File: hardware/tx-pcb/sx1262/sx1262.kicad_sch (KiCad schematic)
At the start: 13 parts, among them U1 SX1262IMLTRT, X1 CS11336-32M

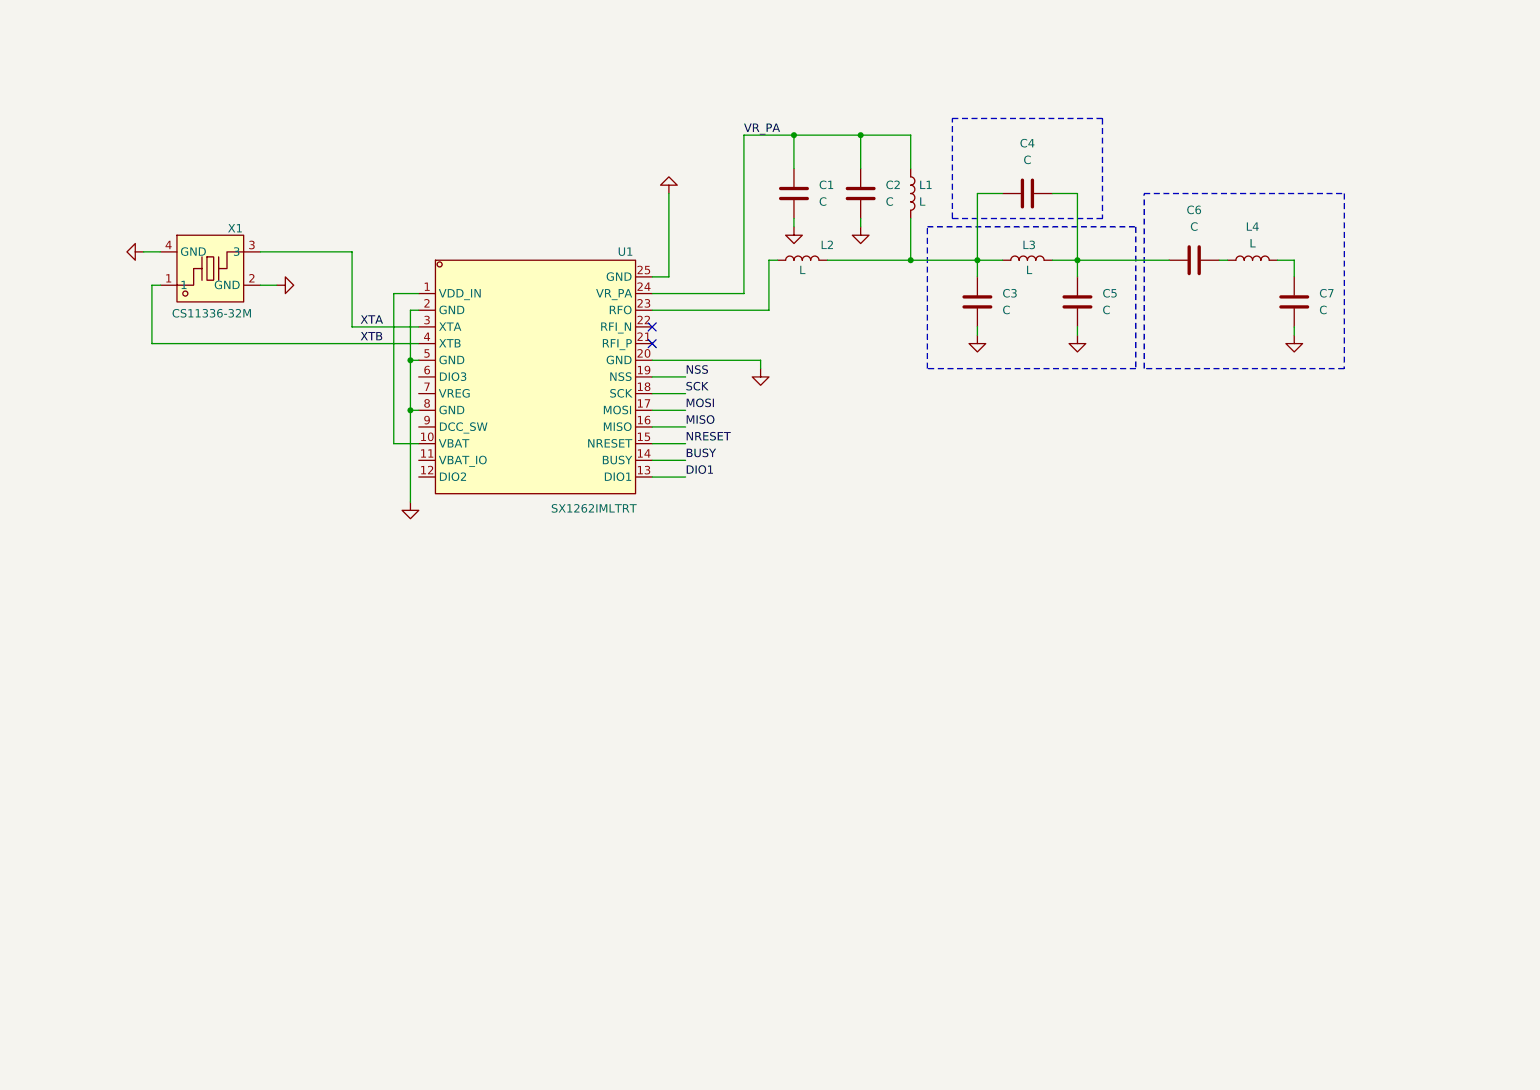
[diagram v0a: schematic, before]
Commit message: added footprints, completed schematics but still need V reg
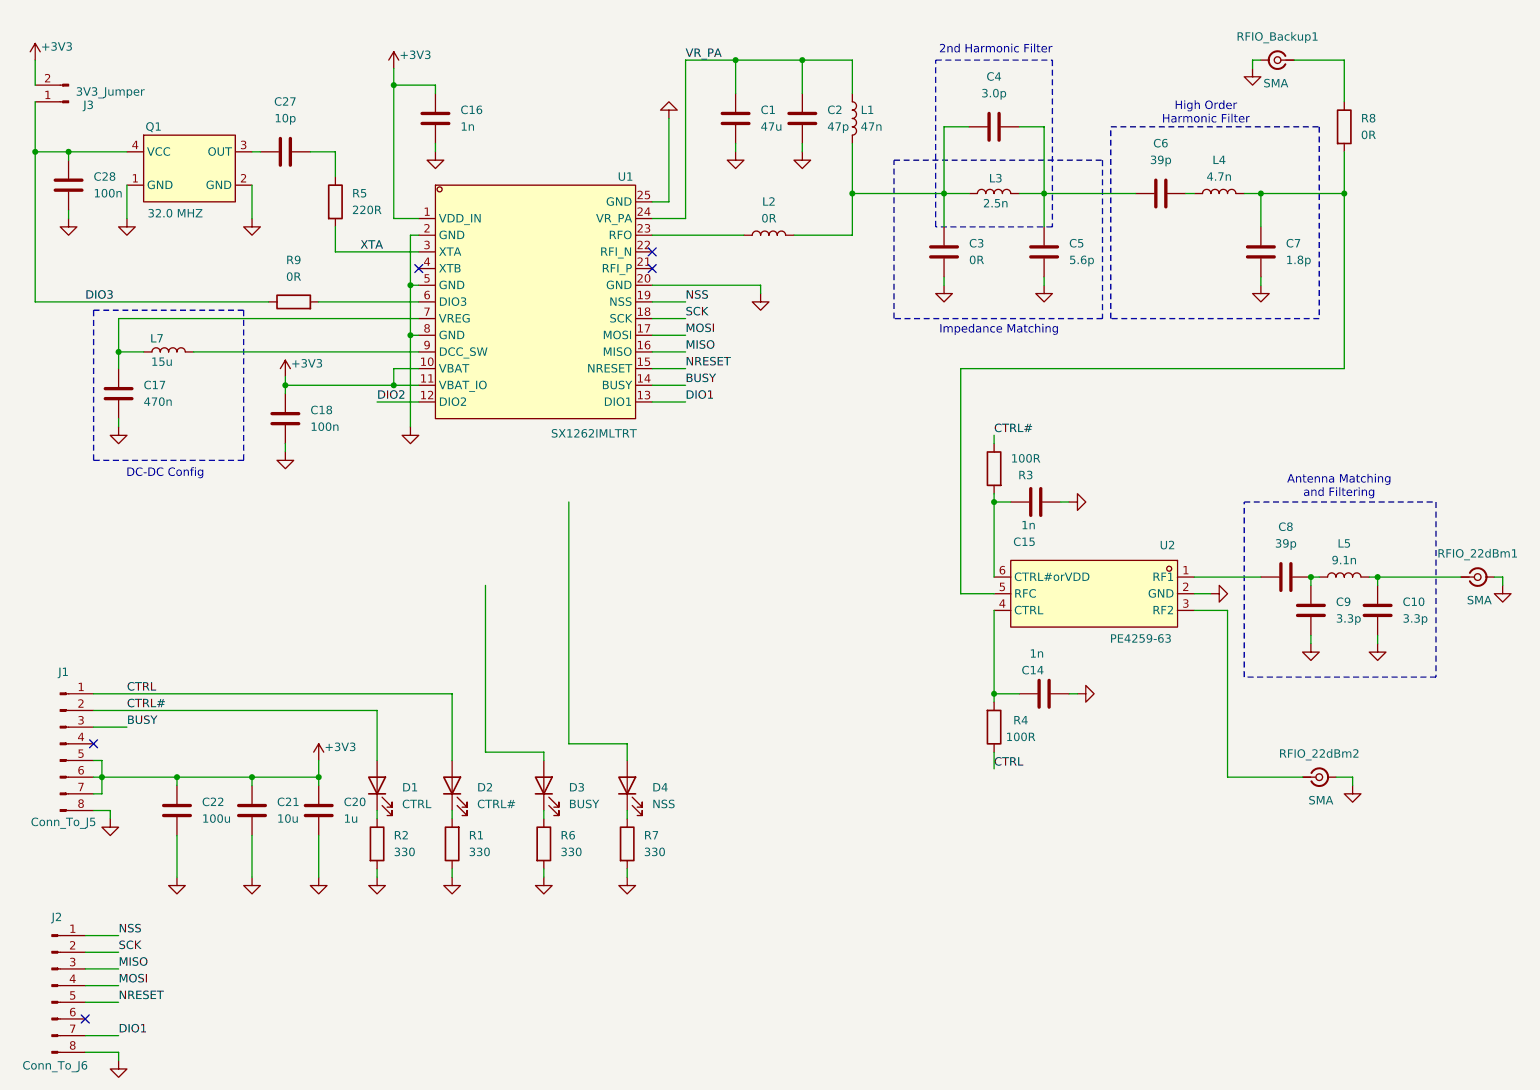
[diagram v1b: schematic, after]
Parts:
- removed X1: CS11336-32M, EasyEDA:NX2016SA_NDK, symbol rx-parts:Q22FA12800025
- added C10, C9: 3.3p, Capacitor_SMD:C_0805_2012Metric_Pad1.18x1.45mm_HandSolder, symbol Device:C
- added C14, C15, C16: 1n, Capacitor_SMD:C_0805_2012Metric_Pad1.18x1.45mm_HandSolder, symbol Device:C
- added C17: 470n, Capacitor_SMD:C_0805_2012Metric_Pad1.18x1.45mm_HandSolder, symbol Device:C
- added C18, C28: 100n, Capacitor_SMD:C_0805_2012Metric_Pad1.18x1.45mm_HandSolder, symbol Device:C
- added C20: 1u, Capacitor_SMD:C_0805_2012Metric_Pad1.18x1.45mm_HandSolder, symbol Device:C
- added C21: 10u, Capacitor_SMD:C_0805_2012Metric_Pad1.18x1.45mm_HandSolder, symbol Device:C
- added C22: 100u, Capacitor_SMD:C_0805_2012Metric_Pad1.18x1.45mm_HandSolder, symbol Device:C
- added C27: 10p, Capacitor_SMD:C_0805_2012Metric_Pad1.18x1.45mm_HandSolder, symbol Device:C
- added C8: 39p, Capacitor_SMD:C_0805_2012Metric_Pad1.18x1.45mm_HandSolder, symbol Device:C
- added D1: CTRL, symbol Device:LED
- added D2: CTRL#, symbol Device:LED
- added D3: BUSY, symbol Device:LED
- added D4: NSS, symbol Device:LED
- added J1: Conn_To_J5, symbol Connector:Conn_01x08_Pin
- added J2: Conn_To_J6, symbol Connector:Conn_01x08_Pin
- added J3: 3V3_Jumper, symbol Connector:Conn_01x02_Pin
- added L5: 9.1n, Inductor_SMD:L_0805_2012Metric_Pad1.05x1.20mm_HandSolder, symbol Device:L
- added L7: 15u, Inductor_SMD:L_0805_2012Metric_Pad1.05x1.20mm_HandSolder, symbol Device:L
- added Q1: 32.0 MHZ, EasyEDA:END4263D_TCXO, symbol easyeda2kicad:END4263D-32M
- added R1, R2, R6, R7: 330, Resistor_SMD:R_0805_2012Metric_Pad1.20x1.40mm_HandSolder, symbol Device:R
- added R3, R4: 100R, Resistor_SMD:R_0805_2012Metric_Pad1.20x1.40mm_HandSolder, symbol Device:R
- added R5: 220R, Resistor_SMD:R_0805_2012Metric_Pad1.20x1.40mm_HandSolder, symbol Device:R
- added R8, R9: 0R, Resistor_SMD:R_0805_2012Metric_Pad1.20x1.40mm_HandSolder, symbol Device:R
- added RFIO_22dBm1, RFIO_22dBm2, RFIO_Backup1: SMA, symbol Connector:Conn_Coaxial_Small
- added U2: PE4259-63, easyeda2kicad:SC-70-6_L2.2-W1.3-P0.65-LS2.1-BL, symbol easyeda2kicad:PE4259-63
- C1: value C -> 47u; footprint (none) -> Capacitor_SMD:C_0805_2012Metric_Pad1.18x1.45mm_HandSolder
- C2: value C -> 47p; footprint (none) -> Capacitor_SMD:C_0805_2012Metric_Pad1.18x1.45mm_HandSolder
- C3: value C -> 0R; footprint (none) -> Capacitor_SMD:C_0805_2012Metric_Pad1.18x1.45mm_HandSolder
- C4: value C -> 3.0p; footprint (none) -> Capacitor_SMD:C_0805_2012Metric_Pad1.18x1.45mm_HandSolder
- C5: value C -> 5.6p; footprint (none) -> Capacitor_SMD:C_0805_2012Metric_Pad1.18x1.45mm_HandSolder
- C6: value C -> 39p; footprint (none) -> Capacitor_SMD:C_0805_2012Metric_Pad1.18x1.45mm_HandSolder
- C7: value C -> 1.8p; footprint (none) -> Capacitor_SMD:C_0805_2012Metric_Pad1.18x1.45mm_HandSolder
- L1: value L -> 47n; footprint (none) -> Inductor_SMD:L_0805_2012Metric_Pad1.05x1.20mm_HandSolder
- L2: value L -> 0R
- L3: value L -> 2.5n; footprint (none) -> Inductor_SMD:L_0805_2012Metric_Pad1.05x1.20mm_HandSolder
- L4: value L -> 4.7n; footprint (none) -> Inductor_SMD:L_0805_2012Metric_Pad1.05x1.20mm_HandSolder
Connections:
- net BUSY: now also J1.3 (Pin_3)
- net DIO1: now also J2.7 (Pin_7)
- net GND: now also C10.2, C14.2, C15.2, C16.2, C17.2, C18.2, C20.2, C21.2, C22.2, C28.1, C9.2, J1.8 (Pin_8), J2.8 (Pin_8), Q1.1 (GND), Q1.2 (GND), R1.1, R2.2, R6.2, R7.2, RFIO_22dBm1.2 (Ext), RFIO_22dBm2.2 (Ext), RFIO_Backup1.2 (Ext), U2.2 (GND)
- net MISO: now also J2.3 (Pin_3)
- net MOSI: now also J2.4 (Pin_4)
- net NRESET: now also J2.5 (Pin_5)
- net NSS: now also J2.1 (Pin_1)
- net SCK: now also J2.2 (Pin_2)
- net XTA: now also R5.2
- net at C7.1, L4.2: now also R8.2, U2.5 (RFC)
- net +3V3: now reaches U1.1 (VDD_IN), U1.10 (VBAT)
- net +3V3: now also U1.11 (VBAT_IO), C16.1, C18.1, C20.1, C21.1, C22.1, J1.5 (Pin_5), J1.6 (Pin_6), J1.7 (Pin_7), J3.2 (Pin_2)
- net DIO2: now reaches U1.12 (DIO2)
- net at U1.6 (DIO3): now also R9.2
- net at U1.7 (VREG): now also C17.1, L7.1
- net at U1.9 (DCC_SW): now also L7.2
- net XTB: no longer names the net of U1.4 (XTB)
- new net: C8.2, C9.1, L5.1
- new net: C10.1, L5.2, RFIO_22dBm1.1 (In)
- new net: D2.1 (K), R1.2
- new net: C14.1, R4.2, U2.4 (CTRL)
- new net: D3.1 (K), R6.1
- new net: D1.1 (K), R2.1
- new net: D4.1 (K), R7.1
- new net: RFIO_22dBm2.1 (In), U2.3 (RF2)
- new net: C27.1, Q1.3 (OUT)
- new net: C27.2, R5.1
- new net: C8.1, U2.1 (RF1)
- new net: C15.1, R3.2, U2.6 (CTRL#orVDD)
- new net: R8.1, RFIO_Backup1.1 (In)
- new net CTRL: D2.2 (A), J1.1 (Pin_1), R4.1
- new net CTRL#: D1.2 (A), J1.2 (Pin_2), R3.1
- new net DIO3: C28.2, J3.1 (Pin_1), Q1.4 (VCC), R9.1
- no-connect marks 2 -> 5
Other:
- note added: "2nd Harmonic Filter"
- note added: "Antenna Matching and Filtering"
- note added: "DC-DC Config"
- note added: "High Order Harmonic Filter"
- note added: "Impedance Matching"
- moved on the sheet: C1, C2, C3, C4, C5, C6, C7, L1, L3, L4, U1

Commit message: made peripheral board for sx1262 module and arranged component layout for pcb
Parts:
- removed J3: 3V3_Jumper, symbol Connector:Conn_01x02_Pin
- added R22: 0R, Resistor_SMD:R_0805_2012Metric_Pad1.20x1.40mm_HandSolder, symbol Device:R
- D1: value CTRL -> RFSW; footprint (none) -> LED_SMD:LED_0805_2012Metric_Pad1.15x1.40mm_HandSolder
- D2: value CTRL# -> RFSW#; footprint (none) -> LED_SMD:LED_0805_2012Metric_Pad1.15x1.40mm_HandSolder
- D3, D4: footprint (none) -> LED_SMD:LED_0805_2012Metric_Pad1.15x1.40mm_HandSolder
- J1: value Conn_To_J5 -> Conn_To_J1; footprint (none) -> Connector_PinHeader_2.54mm:PinHeader_1x08_P2.54mm_Vertical
- J2: value Conn_To_J6 -> Conn_To_J2; footprint (none) -> Connector_PinHeader_2.54mm:PinHeader_1x08_P2.54mm_Vertical
- L2: footprint (none) -> Inductor_SMD:L_0805_2012Metric_Pad1.05x1.20mm_HandSolder
- RFIO_22dBm1, RFIO_22dBm2, RFIO_Backup1: footprint (none) -> Connector_Coaxial:SMA_Amphenol_901-143_Horizontal
- U1: footprint easyeda2kicad:QFN-24_L4.0-W4.0-P0.50-BL-EP2.6 -> EasyEDA:QFN-24_L4.0-W4.0-P0.50-BL-EP2.6
- U2: footprint easyeda2kicad:SC-70-6_L2.2-W1.3-P0.65-LS2.1-BL -> EasyEDA:SC-70-6_L2.2-W1.3-P0.65-LS2.1-BL
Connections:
- net +3V3: now also J2.8 (Pin_8), R22.2; no longer C16.1, J1.5 (Pin_5), J1.6 (Pin_6), J1.7 (Pin_7), U1.1 (VDD_IN)
- net BUSY: now also D3.2 (A), J1.8 (Pin_8); no longer J1.3 (Pin_3)
- net DIO1: now also J2.6 (Pin_6); no longer J2.7 (Pin_7)
- net DIO2: now also J2.5 (Pin_5)
- net GND: now also J1.2 (Pin_2), J2.1 (Pin_1), J2.2 (Pin_2), J2.7 (Pin_7); no longer J1.8 (Pin_8), J2.8 (Pin_8)
- net MISO: now also J1.6 (Pin_6); no longer J2.3 (Pin_3)
- net MOSI: now also J1.5 (Pin_5); no longer J2.4 (Pin_4)
- net NRESET: now also J1.7 (Pin_7); no longer J2.5 (Pin_5)
- net NSS: now also D4.2 (A), J1.3 (Pin_3); no longer J2.1 (Pin_1)
- net SCK: now also J1.4 (Pin_4); no longer J2.2 (Pin_2)
- removed net CTRL: D2.2 (A), J1.1 (Pin_1), R4.1
- removed net CTRL#: D1.2 (A), J1.2 (Pin_2), R3.1
- new net: C16.1, R22.1, U1.1 (VDD_IN)
- new net RFSW: D1.2 (A), J2.4 (Pin_4), R4.1
- new net RFSW#: D2.2 (A), J2.3 (Pin_3), R3.1
- no-connect marks 5 -> 4
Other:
- note added: "Can also use Ferrite Beads instead of R9"
- note added: "MLZ2012N150LT000"
- note added: "RFIC is not being used to receive"
- moved on the sheet: C16, C20, C21, C22, D1, D2, D3, D4, J1, J2, R1, R2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

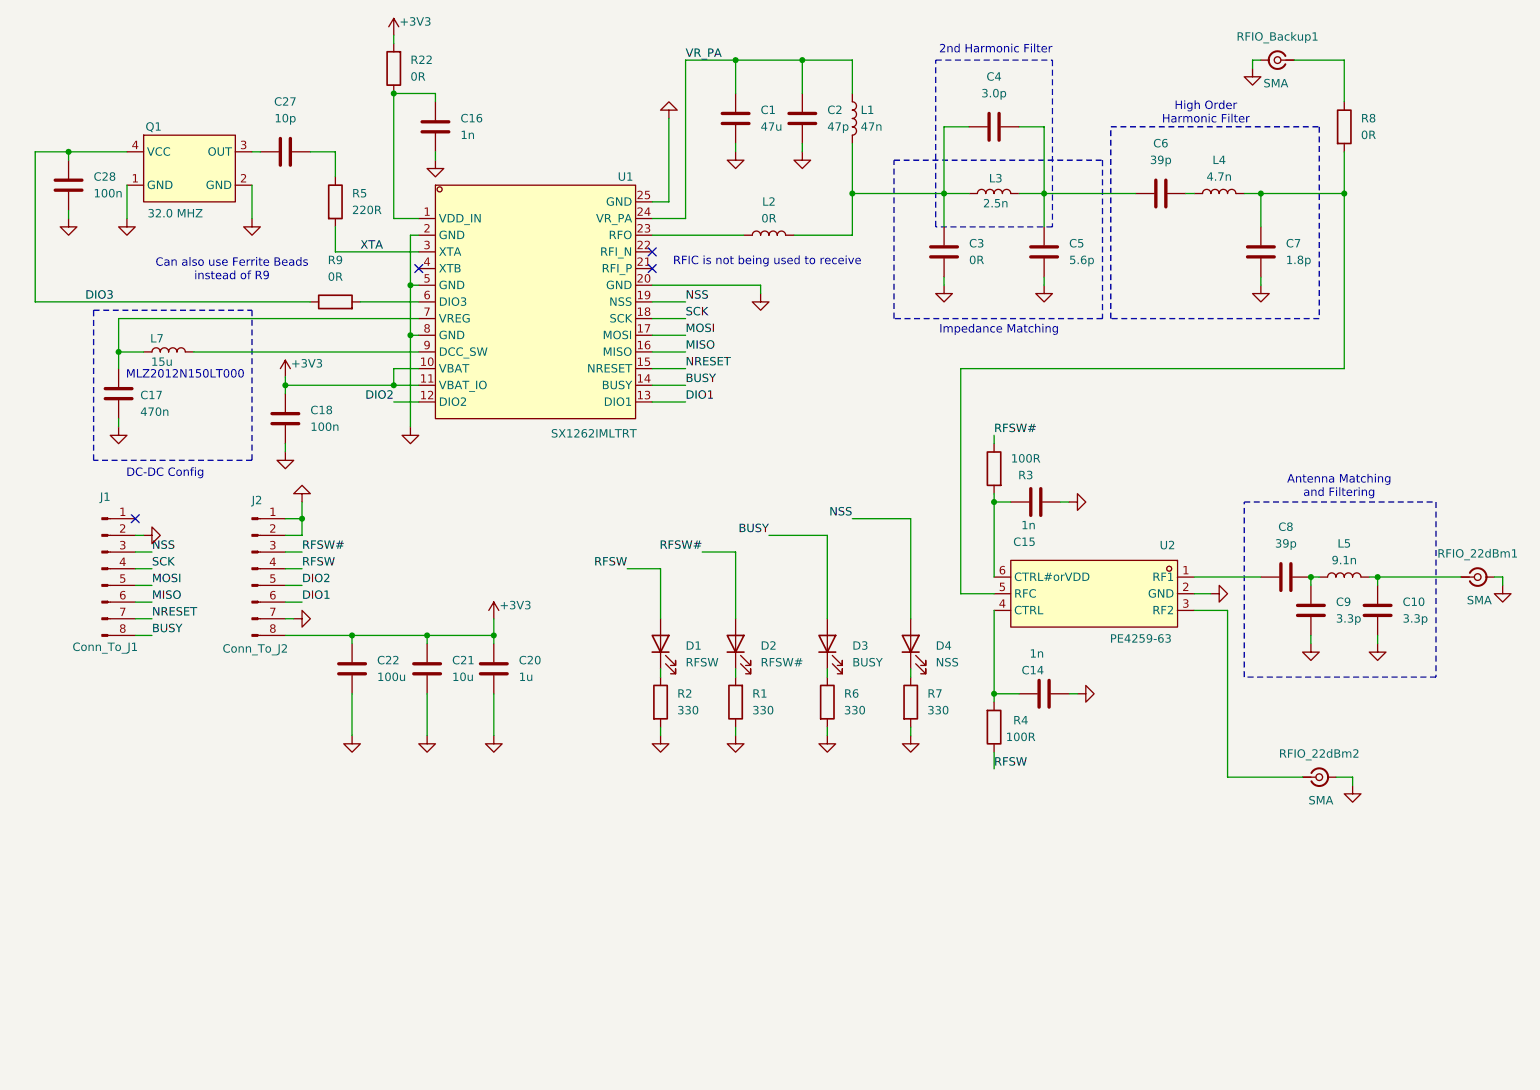
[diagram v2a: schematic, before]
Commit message: replaced TCXO with a normal 32mhz XTAL
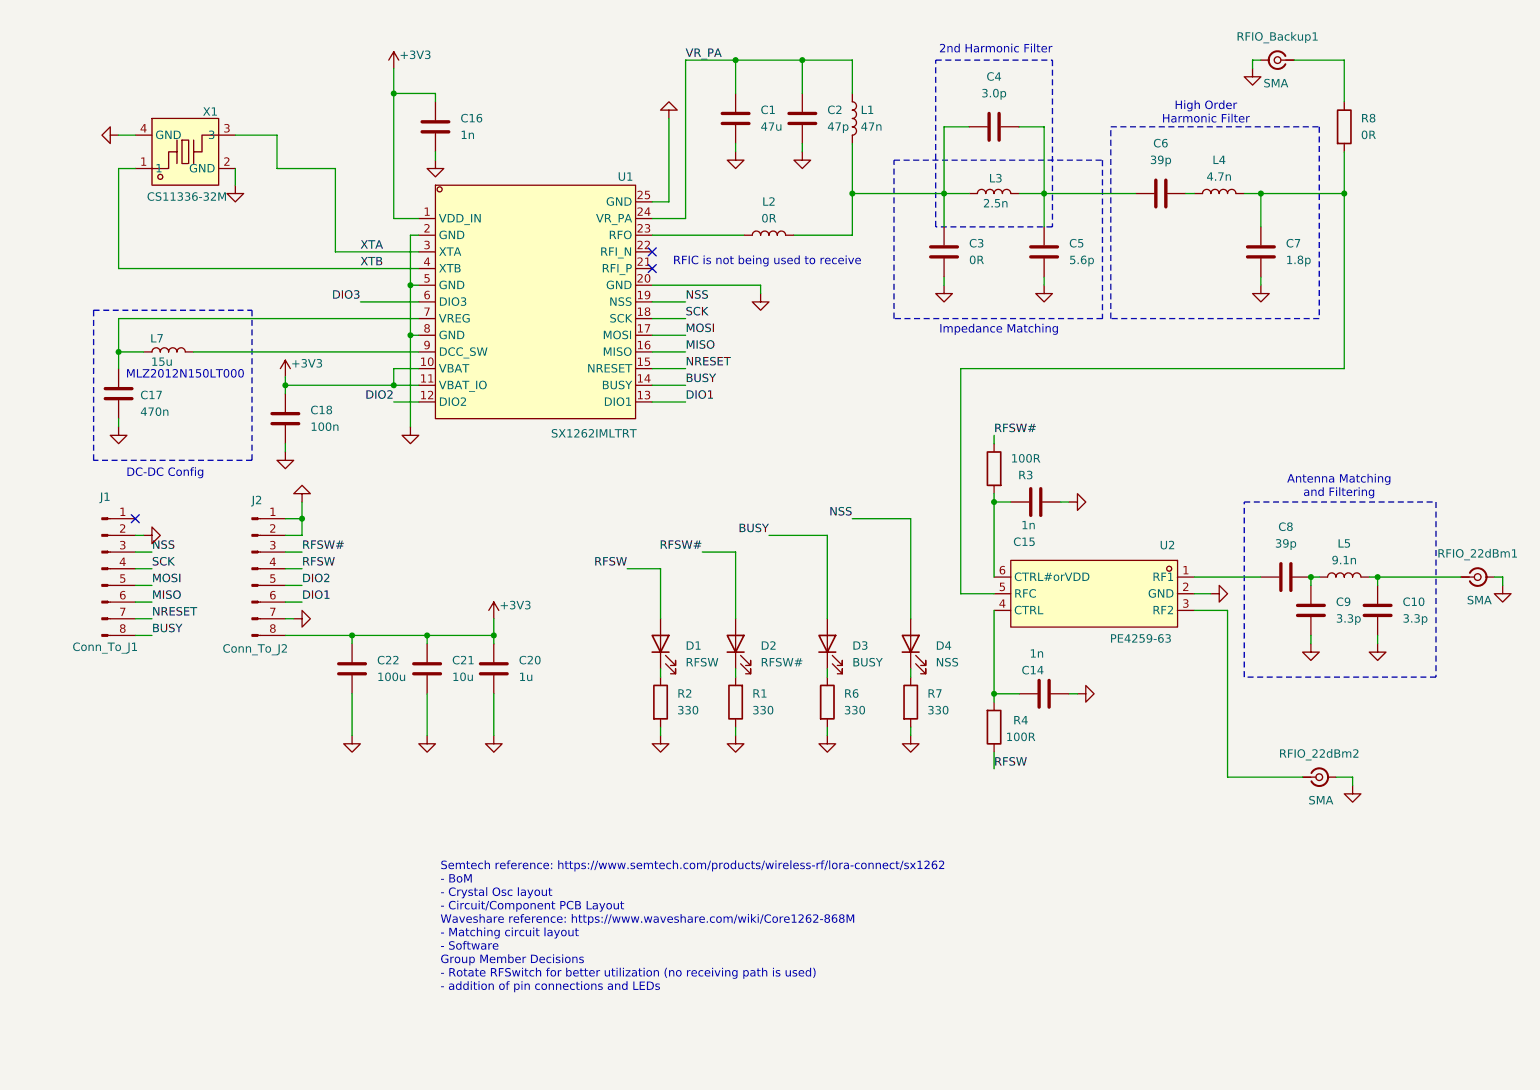
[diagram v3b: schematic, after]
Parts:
- removed C27: 10p, Capacitor_SMD:C_0805_2012Metric_Pad1.18x1.45mm_HandSolder, symbol Device:C
- removed C28: 100n, Capacitor_SMD:C_0805_2012Metric_Pad1.18x1.45mm_HandSolder, symbol Device:C
- removed Q1: 32.0 MHZ, EasyEDA:END4263D_TCXO, symbol easyeda2kicad:END4263D-32M
- removed R22, R9: 0R, Resistor_SMD:R_0805_2012Metric_Pad1.20x1.40mm_HandSolder, symbol Device:R
- removed R5: 220R, Resistor_SMD:R_0805_2012Metric_Pad1.20x1.40mm_HandSolder, symbol Device:R
- added X1: CS11336-32M, rf-lib:NX2016SA_NDK, symbol rx-parts:Q22FA12800025
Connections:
- net +3V3: now also C16.1, U1.1 (VDD_IN)
- net DIO3: now also U1.6 (DIO3)
- net GND: now also X1.2 (GND), X1.4 (GND)
- net XTA: now also X1.3
- net XTB: now reaches U1.4 (XTB)
- net XTB: now also X1.1
- no-connect marks 4 -> 3
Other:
- note added: "Semtech reference: https://www.semtech.com/products/wireless-rf/lora-connect/sx1262 - BoM - Crystal Osc layout - Circuit/Component PCB Layout Waveshare reference: https://www.waveshare.com/wiki/Core1262-868M - Matching circuit layout - Software Group Member Decisions - Rotate RFSwitch for better utilization (no receiving path is used) - addition of pin connections and LEDs"
- note removed: "Can also use Ferrite Beads instead of R9"

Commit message: finished sx1262 receiver PCB design
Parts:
- removed C20: 1u, Capacitor_SMD:C_0805_2012Metric_Pad1.18x1.45mm_HandSolder, symbol Device:C
- removed C22: 100u, Capacitor_SMD:C_0805_2012Metric_Pad1.18x1.45mm_HandSolder, symbol Device:C
